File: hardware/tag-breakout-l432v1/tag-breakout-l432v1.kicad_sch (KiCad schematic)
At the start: 29 parts, among them J1 Conn_01x04_Female, J102 Conn_02x05_Odd_Even, J104 USB_B_Mini, J2 Conn_01x02_Male, SW1 SW_DIP_x04, U1 XC6206, U101 STM32F042K6Tx, U105 Tactile Switch, U2 TS5A3159ADBVR, U4 TS5A3159ADBVR

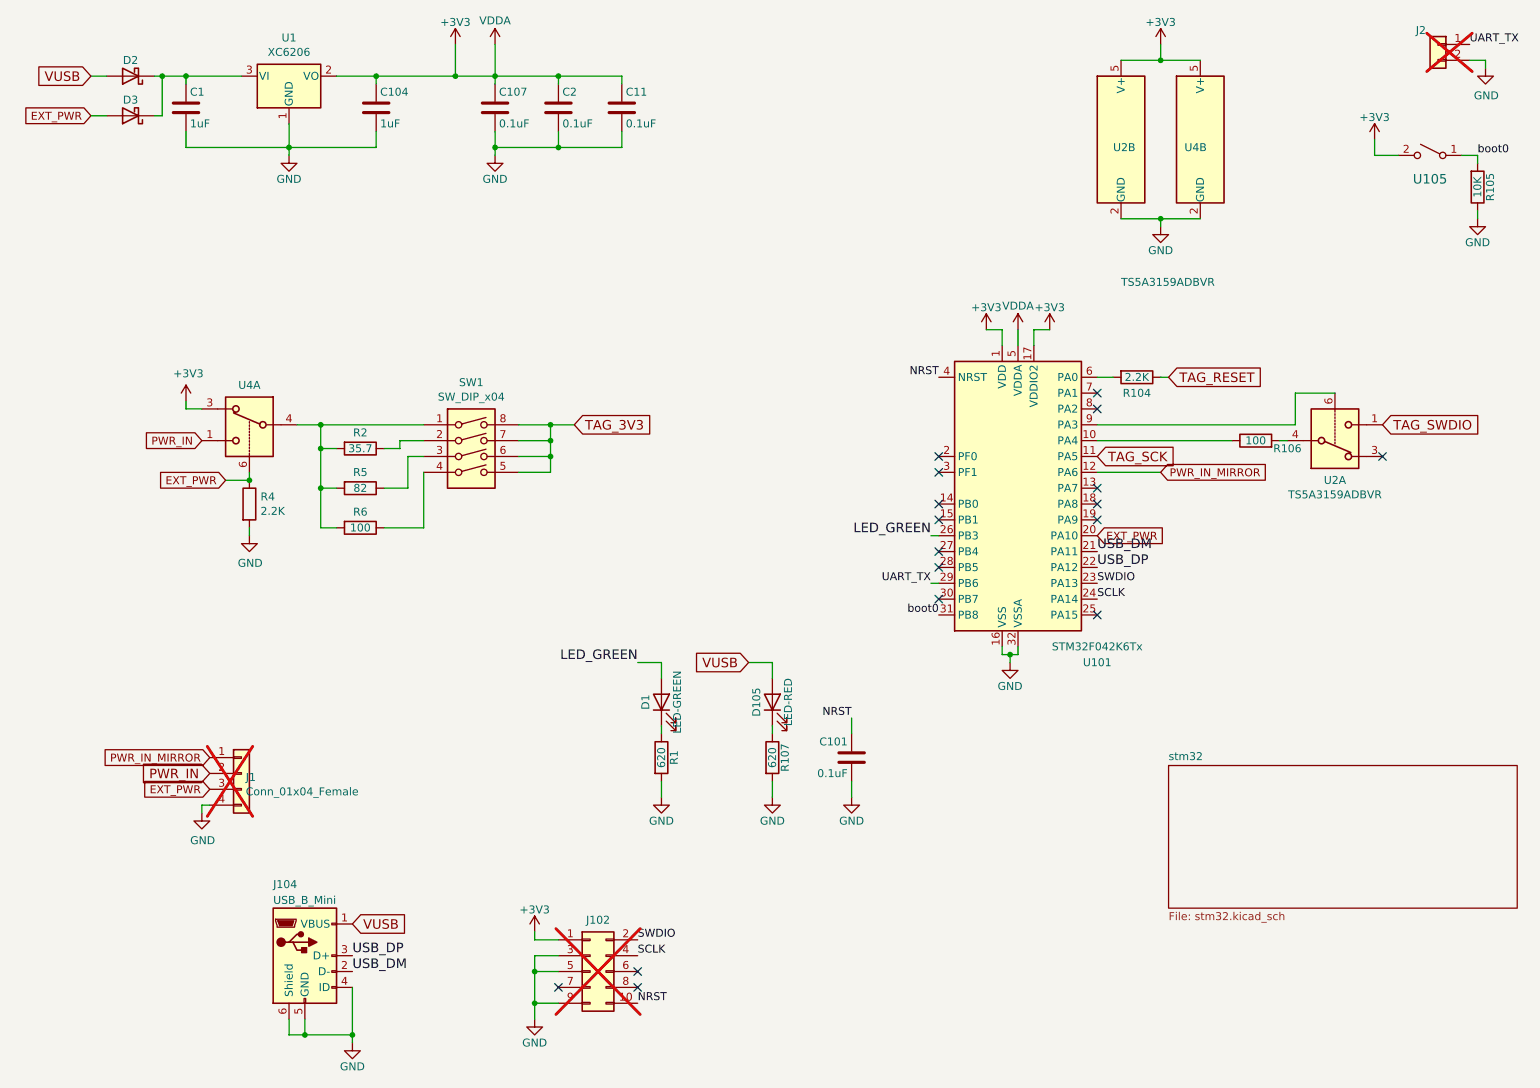
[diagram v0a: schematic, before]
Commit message: checkpoint -- order compass proto board
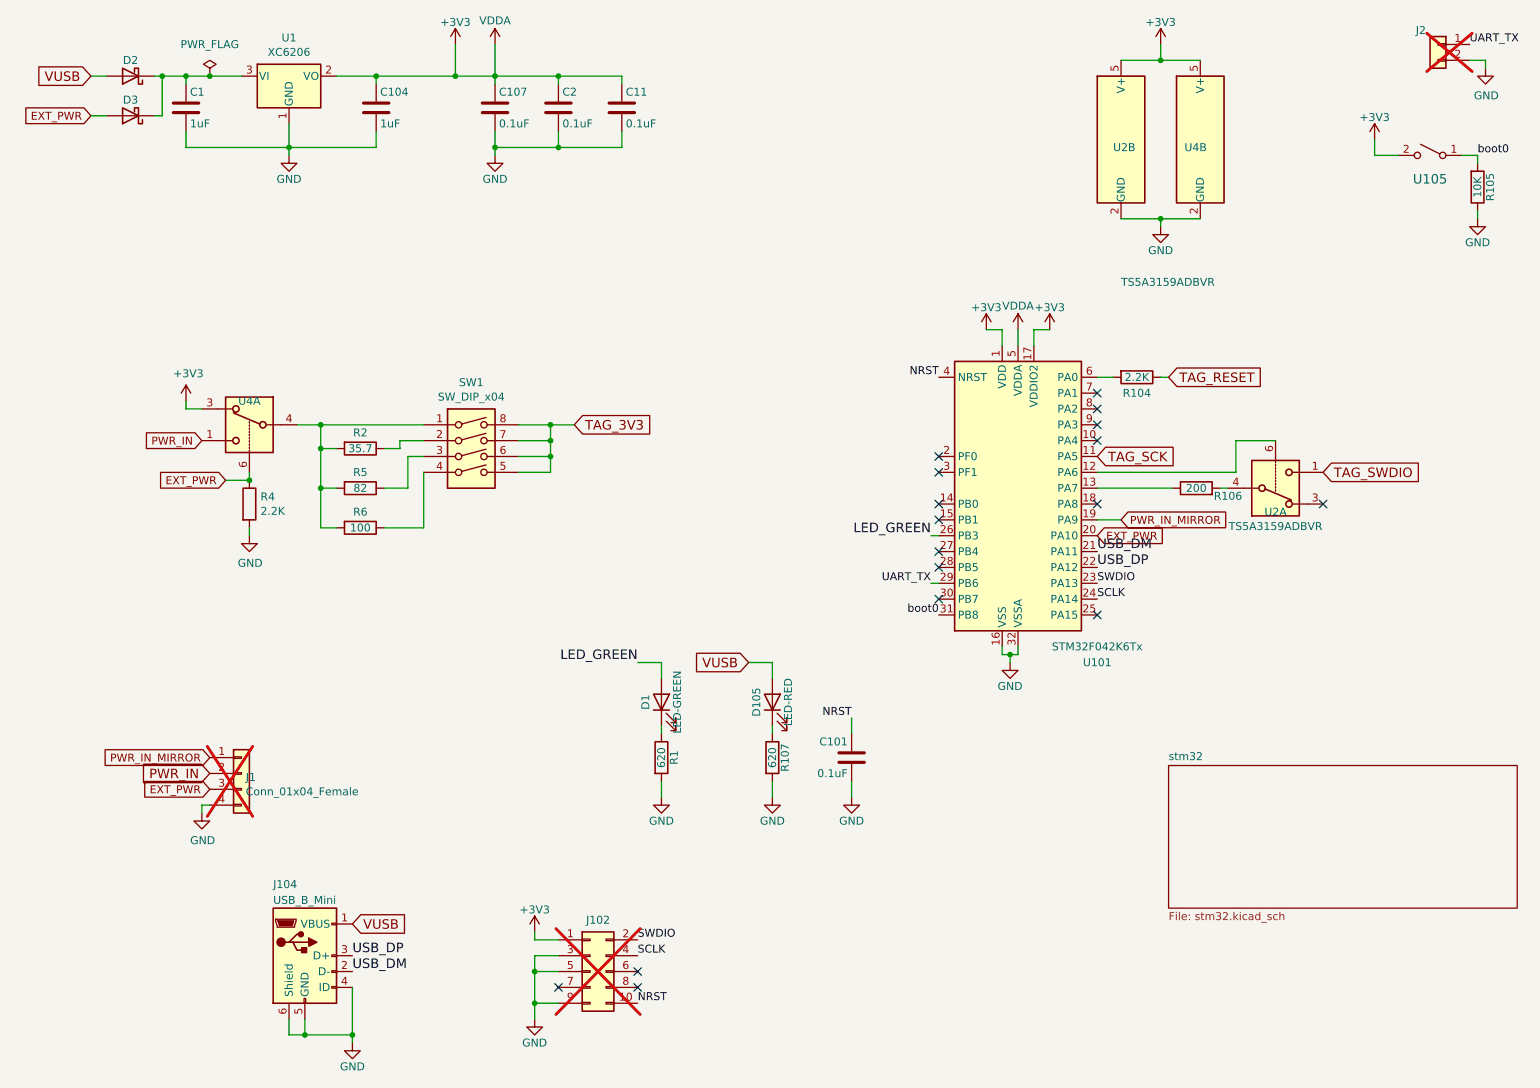
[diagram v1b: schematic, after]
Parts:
- R106: value 100 -> 200; LCSC C22775 -> C8218
- U1: footprint Package_TO_SOT_SMD:SOT-23 -> Package_TO_SOT_SMD:SOT-23-3; symbol Regulator_Linear:MCP1703A-3302_SOT23 -> Regulator_Linear:XC6206PxxxMR
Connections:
- net PWR_IN_MIRROR: now also U101.19 (PA9); no longer U101.12 (PA6)
- net at R106.1: now also U101.13 (PA7); no longer U101.10 (PA4)
- net at U2.6: now also U101.12 (PA6); no longer U101.9 (PA3)
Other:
- moved on the sheet: R106, U2A

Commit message: update proto boards
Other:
- moved on the sheet: R106, U2A
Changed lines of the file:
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@@
 	)
 	(no_connect
-		(at 220.345 97.79)
+		(at 220.98 97.79)
 	)
 	(no_connect
@@
 	(wire
 		(pts
-			(xy 206.375 87.63) (xy 212.725 87.63)
+			(xy 207.01 87.63) (xy 213.36 87.63)
 		)
 		(stroke
@@
 	(wire
 		(pts
-			(xy 203.835 95.25) (xy 205.105 95.25)
+			(xy 204.47 95.25) (xy 205.74 95.25)
 		)
 		(stroke
@@
 	(wire
 		(pts
-			(xy 206.375 87.63) (xy 206.375 92.71)
+			(xy 207.01 87.63) (xy 207.01 92.71)
 		)
 		(stroke
@@
 	(wire
 		(pts
-			(xy 184.15 95.25) (xy 196.215 95.25)
+			(xy 184.15 95.25) (xy 196.85 95.25)
 		)
 		(stroke
@@
 	(wire
 		(pts
-			(xy 184.15 92.71) (xy 206.375 92.71)
+			(xy 184.15 92.71) (xy 207.01 92.71)
 		)
 		(stroke
@@
 	(global_label "TAG_SWDIO"
 		(shape input)
-		(at 220.345 92.71 0)
+		(at 220.98 92.71 0)
 		(fields_autoplaced yes)
 		(effects
@@
 		)
 		(property "Intersheetrefs" "${INTERSHEET_REFS}"
-			(at 235.3337 92.71 0)
+			(at 235.9687 92.71 0)
 			(effects
 				(font
@@
 	(symbol
 		(lib_id "Device:R")
-		(at 200.025 95.25 90)
+		(at 200.66 95.25 90)
 		(unit 1)
 		(exclude_from_sim no)
@@
 		(dnp no)
 		(property "Reference" "R106"
-			(at 205.105 96.52 90)
+			(at 205.74 96.52 90)
 			(effects
 				(font
@@
 		)
 		(property "Value" "200"
-			(at 200.025 95.25 90)
+			(at 200.66 95.25 90)
 			(effects
 				(font
@@
 		)
 		(property "Footprint" "Resistor_SMD:R_0603_1608Metric"
-			(at 200.025 97.028 90)
+			(at 200.66 97.028 90)
 			(effects
 				(font
@@
 		)
 		(property "Datasheet" ""
-			(at 200.025 95.25 0)
+			(at 200.66 95.25 0)
 			(effects
 				(font
@@
 		)
 		(property "Description" ""
-			(at 200.025 95.25 0)
+			(at 200.66 95.25 0)
 			(effects
 				(font
@@
 		)
 		(property "LCSC" "C8218 "
-			(at 296.545 187.96 0)
+			(at 297.18 187.96 0)
 			(effects
 				(font
@@
 		)
 		(property "MFN" "Uniroyal Elec."
-			(at 296.545 187.96 0)
+			(at 297.18 187.96 0)
 			(effects
 				(font
@@
 		)
 		(property "MPN" "0603WAF1000T5E"
-			(at 296.545 187.96 0)
+			(at 297.18 187.96 0)
 			(effects
 				(font
@@
 		)
 		(property "Digikey" ""
-			(at 200.025 95.25 0)
+			(at 200.66 95.25 0)
 			(effects
 				(font
@@
 	(symbol
 		(lib_id "Analog_Switch:TS5A3159ADBVR")
-		(at 212.725 95.25 0)
+		(at 213.36 95.25 0)
 		(mirror x)
 		(unit 1)
@@
 		(dnp no)
 		(property "Reference" "U2"
-			(at 212.725 99.06 0)
+			(at 213.36 99.06 0)
 			(effects
 				(font
@@
 		)
 		(property "Value" "TS5A3159ADBVR"
-			(at 212.725 101.3714 0)
+			(at 213.36 101.3714 0)
 			(effects
 				(font
@@
 		)
 		(property "Footprint" "Package_TO_SOT_SMD:SOT-23-6"
-			(at 212.725 87.63 0)
+			(at 213.36 87.63 0)
 			(effects
 				(font
@@
 		)
 		(property "Datasheet" "http://www.ti.com/lit/ds/symlink/ts5a3159a.pdf"
-			(at 212.725 95.25 0)
+			(at 213.36 95.25 0)
 			(effects
 				(font
@@
 		)
 		(property "Description" "Single SPDT Analog Switch, 1.65-V to 5.5-V Single-Supply Operation, 1Ohm Ron, SOT-23-6"
-			(at 212.725 95.25 0)
+			(at 213.36 95.25 0)
 			(effects
 				(font
@@
 		)
 		(property "MFN" "TI"
-			(at 212.725 95.25 0)
+			(at 213.36 95.25 0)
 			(effects
 				(font
@@
 		)
 		(property "MPN" "TS5A3159ADBVR"
-			(at 212.725 95.25 0)
+			(at 213.36 95.25 0)
 			(effects
 				(font
@@
 		)
 		(property "LCSC" "C128405"
-			(at 212.725 95.25 0)
+			(at 213.36 95.25 0)
 			(effects
 				(font
@@
 		)
 		(property "Digikey" ""
-			(at 212.725 95.25 0)
+			(at 213.36 95.25 0)
 			(effects
 				(font
@@
 			)
 		)
-		(property "Datasheet" ""
+		(property "Datasheet" "~"
 			(at 60.96 171.45 0)
 			(effects
@@
 			)
 		)
-		(property "Description" "CONN RCPT USB2.0 MINI B SMD R/A"
+		(property "Description" "USB Mini Type B connector"
 			(at 57.15 170.18 0)
 			(effects
@@
 		(at 195.58 139.7)
 		(size 55.88 22.86)
-		(fields_autoplaced yes)
 		(stroke
 			(width 0)
@@
 		)
 		(property "Sheetname" "stm32"
-			(at 195.58 138.9884 0)
+			(at 195.58 138.43 0)
 			(effects
 				(font
